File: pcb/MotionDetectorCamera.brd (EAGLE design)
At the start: 64.8 x 50.8 mm, 129 parts, among them J2 S-MOUNT-LENS-HOLDER, U1 LATTICE-ICE40HX4K-BG121, U10 NXP-NTB0102, U11 ON-NLAS3157, U12 ON-NLAS3157, U13 STM-STM32F730, U2 TI-TPS6280XYKAR, U3 MICROSD-SOCKET, U4 TI-TPS6280XYKAR, U5 W989D6DBGX6I, U6 TI-TPS63805YFFR, U8 ON-AR0330CS1C12SPKA0, U9 TI-TMUX1574, X1 SITIME-SIT8021, X2 SITIME-SIT8021

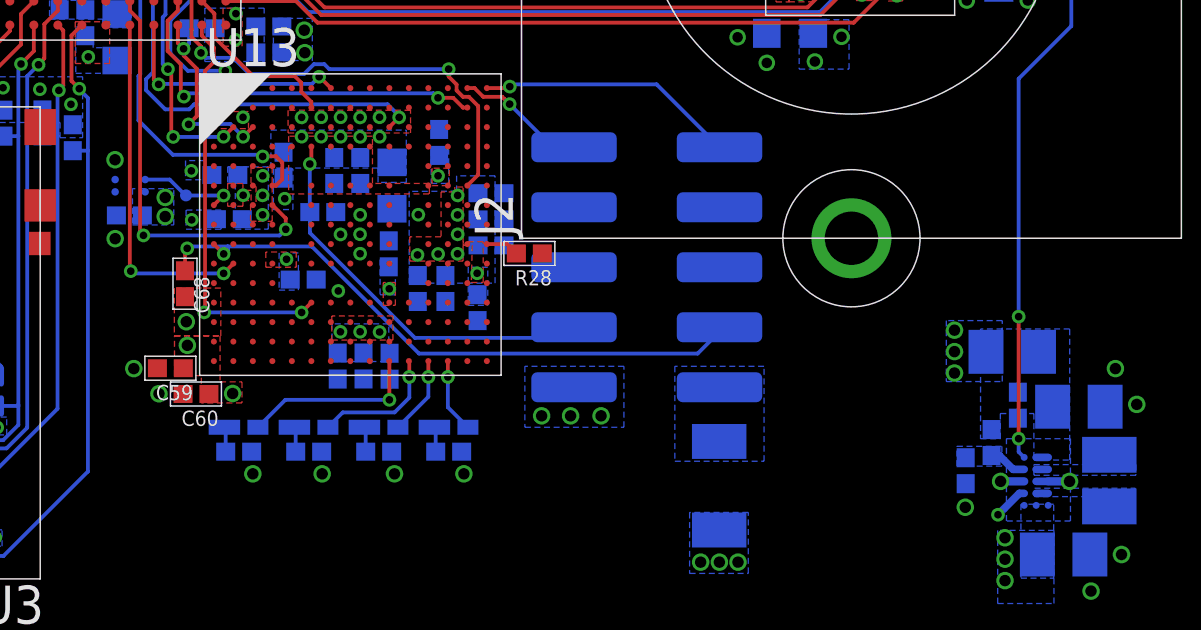
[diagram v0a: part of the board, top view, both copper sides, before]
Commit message: Fixed all DRC errors
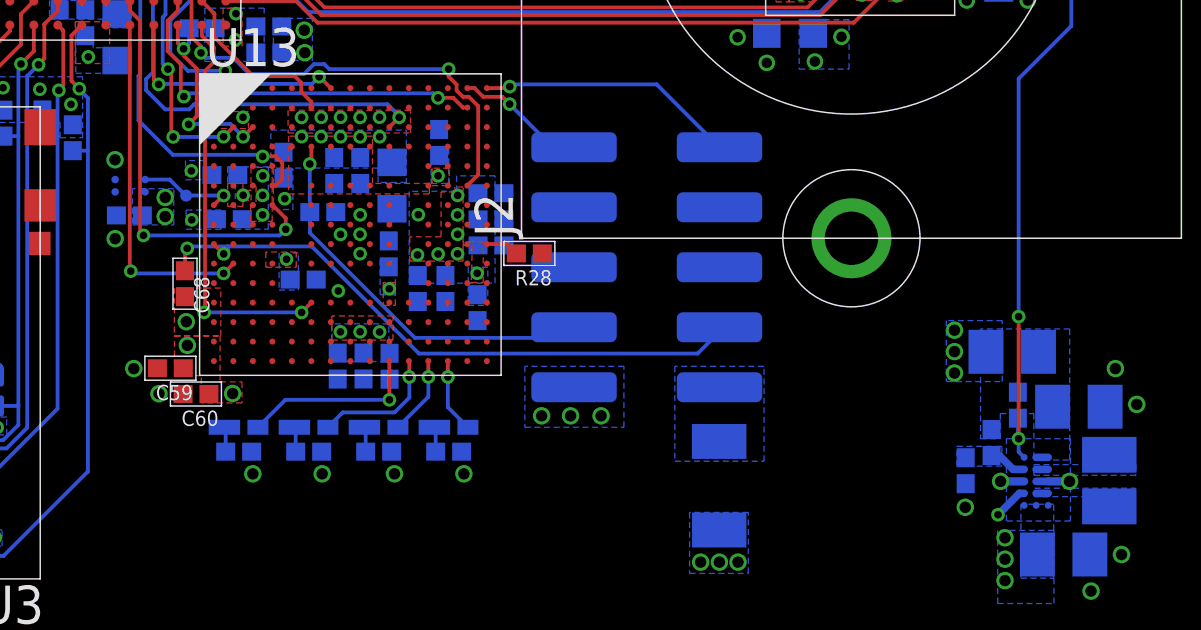
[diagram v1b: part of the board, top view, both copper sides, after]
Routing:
- net 2V8GOOD: track 41.0 -> 41.7 mm
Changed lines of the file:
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@@
 <attribute name="PN" value="SIT8021AI-J4-18S-24.000000E" x="20.6502" y="18.2118" size="1.778" layer="28" rot="MR270" display="off"/>
 </element>
-<element name="TP10" library="EagleLibrary" package="TEST-POINT" value="TEST-POINT" x="20.200621875" y="17.88921875" smashed="yes" rot="MR180">
-<attribute name="NAME" x="20.200621875" y="17.56221875" size="0.508" layer="26" font="vector" rot="MR180" align="bottom-center"/>
+<element name="TP10" library="EagleLibrary" package="TEST-POINT" value="TEST-POINT" x="20.205703125" y="17.881596875" smashed="yes" rot="MR180">
+<attribute name="NAME" x="20.205703125" y="17.554596875" size="0.508" layer="26" font="vector" rot="MR180" align="bottom-center"/>
 </element>
 <element name="L4" library="EagleLibrary" package="0806" package3d_urn="urn:adsk.eagle:package:22485740/1" value="470n" x="24.5364" y="37.0179625" smashed="yes" rot="MR0">
@@
 <wire x1="48.1394" y1="9.1566" x2="47.9552" y2="9.3408" width="0.127" layer="16"/>
 <wire x1="47.9552" y1="9.3408" x2="47.9552" y2="9.779" width="0.127" layer="16"/>
-<wire x1="47.9552" y1="9.779" x2="47.9298" y2="10.4641" width="0" layer="19" extent="16-16"/>
+<wire x1="47.9552" y1="9.779" x2="47.9298" y2="9.779" width="0.127" layer="16"/>
+<wire x1="47.9298" y1="9.779" x2="47.9298" y2="10.4641" width="0.127" layer="16"/>
 </signal>
 <signal name="SD_CLK">
@@
 <signal name="STM_CLK24MHZ">
 <contactref element="X2" pad="2"/>
-<contactref element="TP10" pad="X"/>
 <contactref element="U13" pad="G1"/>
 <via x="21.45508125" y="17.886403125" extent="1-16" drill="0.254"/>
@@
 <wire x1="21.1294" y1="17.5664" x2="21.449403125" y2="17.886403125" width="0.127" layer="1"/>
 <wire x1="21.449403125" y1="17.886403125" x2="21.45508125" y2="17.886403125" width="0.127" layer="1"/>
-<wire x1="20.18700625" y1="17.886403125" x2="21.45508125" y2="17.886403125" width="0.127" layer="16"/>
-<wire x1="21.1294" y1="17.5664" x2="20.200621875" y2="17.88921875" width="0" layer="19" extent="1-16"/>
+<wire x1="20.18700625" y1="17.886403125" x2="20.205703125" y2="17.886403125" width="0.127" layer="16"/>
+<contactref element="TP10" pad="X"/>
+<wire x1="20.205703125" y1="17.886403125" x2="21.45508125" y2="17.886403125" width="0.127" layer="16"/>
+<wire x1="20.205703125" y1="17.881596875" x2="20.205703125" y2="17.886403125" width="0.127" layer="16"/>
 </signal>
 <signal name="N$1">

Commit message: Layout progress
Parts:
- moved C18 0.36 mm to (22.6, 38.5)
- moved C37 0.36 mm to (47.0, 25.3)
- moved C39 0.36 mm to (42.4, 30.5)
- moved C41 0.36 mm to (38.0, 24.8)
- moved C43 0.36 mm to (46.0, 25.3)
- moved L4 0.36 mm to (24.3, 36.8)
- moved R12 0.36 mm to (31.3, 34.6)
- moved R6 0.36 mm to (22.6, 34.8)
- moved C26 0.36 mm to (10.6, 33.4)
- moved H1 0.36 mm to (35.3, 15.2)
- moved L2 0.36 mm to (50.7, 8.13)
- moved R18 0.36 mm to (46.8, 9.40)
- moved C13 0.36 mm to (16.5, 28.6)
- moved C15 0.36 mm to (16.5, 27.6)
- moved C17 0.36 mm to (16.0, 26.2)
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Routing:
- net GND: vias 96 -> 97
- net 2V8: vias 26 -> 27
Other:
- board size 64.8 x 50.8 mm -> 55.9 x 44.5 mm
- board text added: "MDC Rev 3"
- board text removed: "MDC Rev 2"

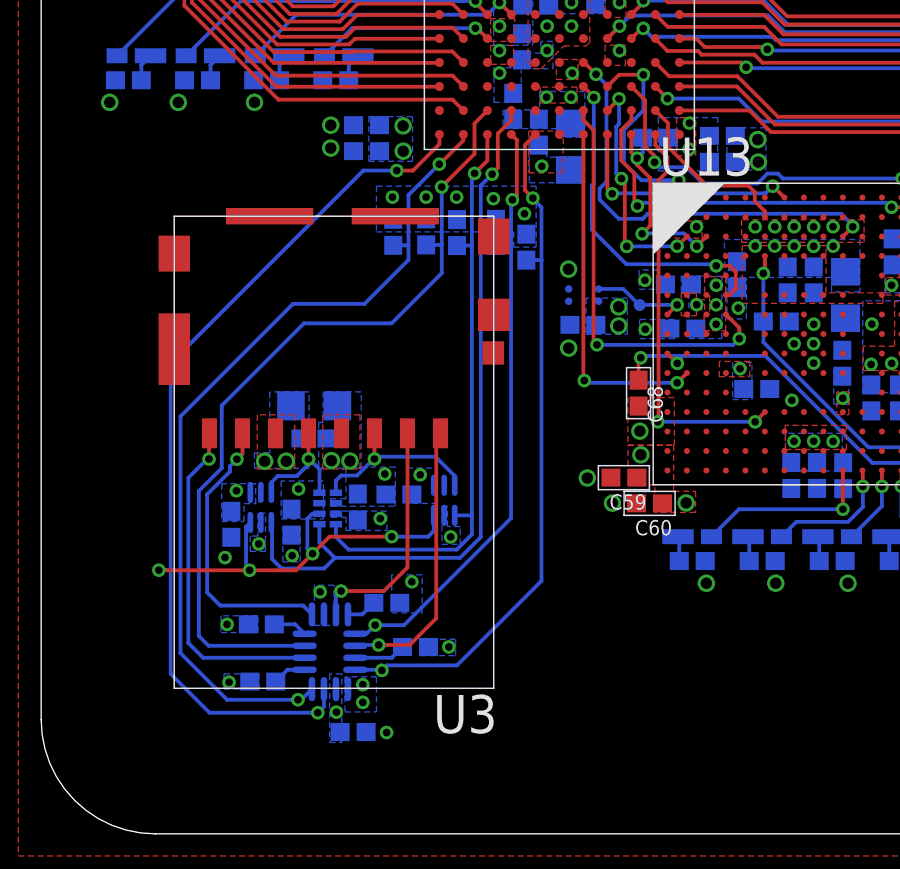
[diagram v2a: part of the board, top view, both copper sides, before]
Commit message: Use wires instead of polygons on power signals on pullups
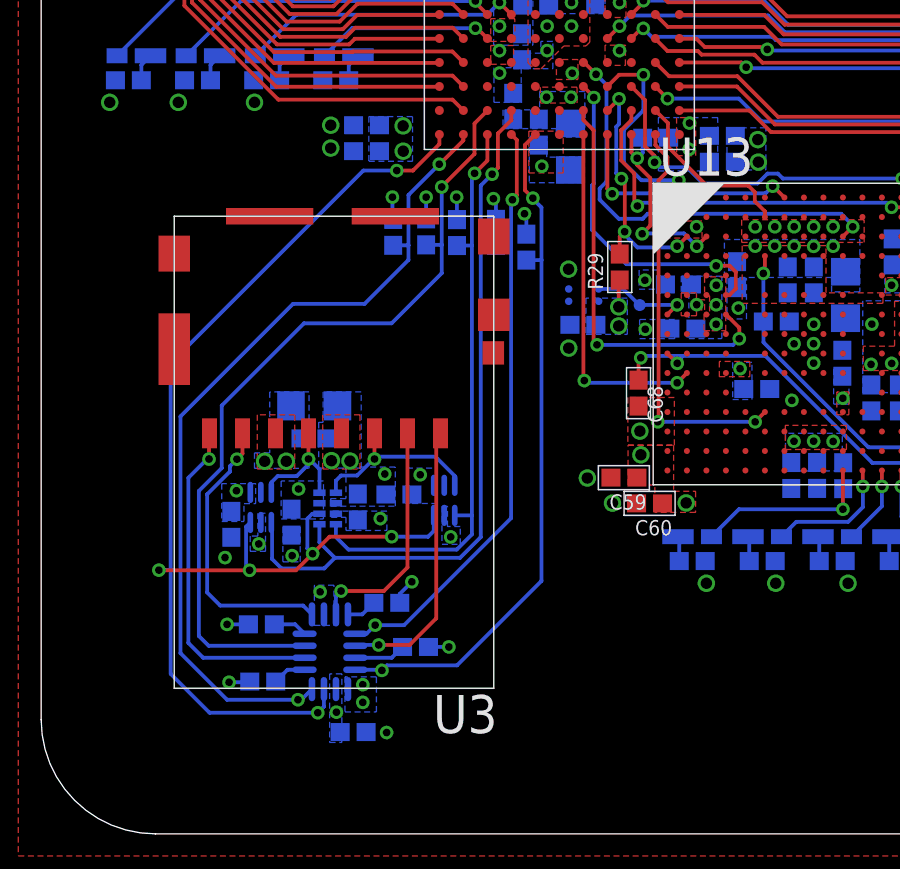
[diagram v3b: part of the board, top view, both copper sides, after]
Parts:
- added R29: 10k, EagleLibrary:0402
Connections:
- net 1V8: now also R29.1
- net ICE_CDONE: now also R29.2
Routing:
- net 1V8: track 0.35 -> 4.92 mm
- net 2V8: track 0.84 -> 3.80 mm
- net ICE_CDONE: track 7.79 -> 8.45 mm
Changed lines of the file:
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@@
 <attribute name="PN" value="GRM155R61H104KE19D" x="10.398759375" y="7.203440625" size="1.778" layer="28" rot="MR180" display="off"/>
+</element>
+<element name="R29" library="EagleLibrary" package="0402" package3d_urn="urn:adsk.eagle:package:17080064/1" value="10k" x="19.286221875" y="18.8950625" smashed="yes" rot="R90">
+<attribute name="MFG" value="Vishay" x="19.286221875" y="18.8950625" size="1.778" layer="27" rot="R90" display="off"/>
+<attribute name="NAME" x="18.730221875" y="18.1410625" size="0.508" layer="25" font="vector" rot="R90"/>
+<attribute name="PN" value="CRCW040210K0FKEDC" x="19.286221875" y="18.8950625" size="1.778" layer="27" rot="R90" display="off"/>
 </element>
 </elements>
@@
 <via x="13.84808125" y="21.224240625" extent="1-16" drill="0.254"/>
 <via x="15.074903125" y="21.173440625" extent="1-16" drill="0.254"/>
-<polygon width="0.127" layer="16" thermals="no" rank="2">
-<vertex x="11.176" y="21.59"/>
-<vertex x="11.176" y="20.066"/>
-<vertex x="15.748" y="20.066"/>
-<vertex x="15.748" y="19.558"/>
-<vertex x="16.499840625" y="19.558"/>
-<vertex x="16.499840625" y="21.59"/>
-</polygon>
 <via x="16.11121875" y="20.67051875" extent="1-16" drill="0.254"/>
 <polygon width="0.127" layer="16" thermals="no">
@@
 <vertex x="7.406640625" y="39.756078125"/>
 </polygon>
+<contactref element="R29" pad="1"/>
+<wire x1="19.286221875" y1="18.4625625" x2="19.2532" y2="18.429540625" width="0.127" layer="1"/>
+<wire x1="19.2532" y1="18.429540625" x2="19.2532" y2="17.566640625" width="0.127" layer="1"/>
+<wire x1="11.7348" y1="20.4832625" x2="11.709403125" y2="20.508659375" width="0.127" layer="16"/>
+<wire x1="11.709403125" y1="20.508659375" x2="11.709403125" y2="21.224240625" width="0.127" layer="16"/>
+<wire x1="12.832075" y1="20.4985" x2="12.832075" y2="21.224234375" width="0.127" layer="16"/>
+<wire x1="12.832075" y1="21.224234375" x2="12.83208125" y2="21.224240625" width="0.127" layer="16"/>
+<wire x1="13.8614125" y1="20.4756375" x2="13.8614125" y2="21.210909375" width="0.127" layer="16"/>
+<wire x1="13.8614125" y1="21.210909375" x2="13.84808125" y2="21.224240625" width="0.127" layer="16"/>
+<wire x1="15.160940625" y1="20.483259375" x2="15.160940625" y2="21.087403125" width="0.127" layer="16"/>
+<wire x1="15.160940625" y1="21.087403125" x2="15.074903125" y2="21.173440625" width="0.127" layer="16"/>
+<wire x1="16.17345" y1="19.9905" x2="16.17345" y2="20.6082875" width="0.127" layer="16"/>
+<wire x1="16.17345" y1="20.6082875" x2="16.11121875" y2="20.67051875" width="0.127" layer="16"/>
 </signal>
 <signal name="GND">
@@
 <via x="8.58011875" y="11.49604375" extent="1-16" drill="0.254"/>
 <via x="12.3571" y="8.402321875" extent="1-16" drill="0.254"/>
-<polygon width="0.127" layer="16" thermals="no">
-<vertex x="11.684" y="8.636"/>
-<vertex x="11.684" y="7.366"/>
-<vertex x="12.7" y="7.366"/>
-<vertex x="12.7" y="8.636"/>
-</polygon>
 <via x="6.1976" y="6.982459375" extent="1-16" drill="0.254"/>
 <via x="6.263640625" y="5.0546" extent="1-16" drill="0.254"/>
-<polygon width="0.127" layer="16" thermals="no">
-<vertex x="5.9944" y="7.26948125"/>
-<vertex x="5.9944" y="6.71068125"/>
-<vertex x="7.2288375" y="6.71068125"/>
-<vertex x="7.2288375" y="7.26948125"/>
-</polygon>
-<polygon width="0.127" layer="16" thermals="no">
-<vertex x="6.096" y="5.334"/>
-<vertex x="6.096" y="4.826"/>
-<vertex x="7.261859375" y="4.826"/>
-<vertex x="7.261859375" y="5.334"/>
-</polygon>
 <polygon width="0.127" layer="15" thermals="no">
 <vertex x="4.2672" y="12.7762"/>
@@
 <via x="45.562521875" y="11.714478125" extent="1-16" drill="0.381"/>
 <via x="13.591540625" y="6.23061875" extent="1-16" drill="0.254"/>
-<polygon width="0.127" layer="16" thermals="no">
-<vertex x="12.61871875" y="6.487159375"/>
-<vertex x="12.61871875" y="5.941059375"/>
-<vertex x="13.815059375" y="5.941059375"/>
-<vertex x="13.815059375" y="6.487159375"/>
-</polygon>
 <via x="39.309140625" y="30.6451" extent="1-16" drill="0.381"/>
+<wire x1="6.9081" y1="6.985" x2="6.905559375" y2="6.982459375" width="0.127" layer="16"/>
+<wire x1="6.905559375" y1="6.982459375" x2="6.1976" y2="6.982459375" width="0.127" layer="16"/>
+<wire x1="6.95381875" y1="5.077459375" x2="6.930959375" y2="5.0546" width="0.127" layer="16"/>
+<wire x1="6.930959375" y1="5.0546" x2="6.263640625" y2="5.0546" width="0.127" layer="16"/>
+<wire x1="12.91151875" y1="6.23061875" x2="13.591540625" y2="6.23061875" width="0.127" layer="16"/>
+<wire x1="11.953940625" y1="7.70128125" x2="11.953940625" y2="7.9991625" width="0.127" layer="16"/>
+<wire x1="11.953940625" y1="7.9991625" x2="12.3571" y2="8.402321875" width="0.127" layer="16"/>
 </signal>
 <signal name="N$12">
@@
 <via x="19.344640625" y="21.844" extent="1-16" drill="0.254"/>
 <wire x1="19.344640625" y1="21.844" x2="19.456396875" y2="21.73224375" width="0.127" layer="1"/>
-<wire x1="19.456396875" y1="21.73224375" x2="19.456396875" y2="19.6469" width="0.127" layer="1"/>
-<wire x1="19.456396875" y1="19.6469" x2="19.519896875" y2="19.5834" width="0.127" layer="1"/>
-<via x="19.519896875" y="19.5834" extent="1-16" drill="0.254"/>
-<wire x1="21.198840625" y1="19.591021875" x2="21.19121875" y2="19.5834" width="0.127" layer="16"/>
-<wire x1="21.19121875" y1="19.5834" x2="19.519896875" y2="19.5834" width="0.127" layer="16"/>
+<wire x1="19.456396875" y1="21.73224375" x2="19.456396875" y2="20.081240625" width="0.127" layer="1"/>
+<wire x1="19.456396875" y1="20.081240625" x2="19.448775" y2="20.07361875" width="0.127" layer="1"/>
+<via x="19.448775" y="20.07361875" extent="1-16" drill="0.254"/>
+<wire x1="21.198840625" y1="19.591021875" x2="21.155659375" y2="19.547840625" width="0.127" layer="16"/>
+<wire x1="21.155659375" y1="19.547840625" x2="19.87549375" y2="19.547840625" width="0.127" layer="16"/>
+<wire x1="19.87549375" y1="19.547840625" x2="19.448775" y2="19.974559375" width="0.127" layer="16"/>
+<wire x1="19.448775" y1="19.974559375" x2="19.448775" y2="20.07361875" width="0.127" layer="16"/>
 <contactref element="U13" pad="C2"/>
 <wire x1="21.5254" y1="19.9124" x2="21.204021875" y2="19.591021875" width="0.127" layer="1"/>
 <wire x1="21.204021875" y1="19.591021875" x2="21.198840625" y2="19.591021875" width="0.127" layer="1"/>
+<contactref element="R29" pad="2"/>
+<wire x1="19.286221875" y1="19.3275625" x2="19.286221875" y2="19.911065625" width="0.127" layer="1"/>
+<wire x1="19.286221875" y1="19.911065625" x2="19.448775" y2="20.07361875" width="0.127" layer="1"/>
 </signal>
 <signal name="ICE_CRST_">

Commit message: Switch back to 56k pullups on SD card lines
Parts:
- C28, C29: device EagleLibrary:0805 -> EagleLibrary:0805@1
- R10, R11, R24, R25, R26, R27, R7, R8, R9: value 100k -> 56k
